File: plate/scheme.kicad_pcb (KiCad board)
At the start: 2 copper layers, 50 x 100 mm, 9 parts

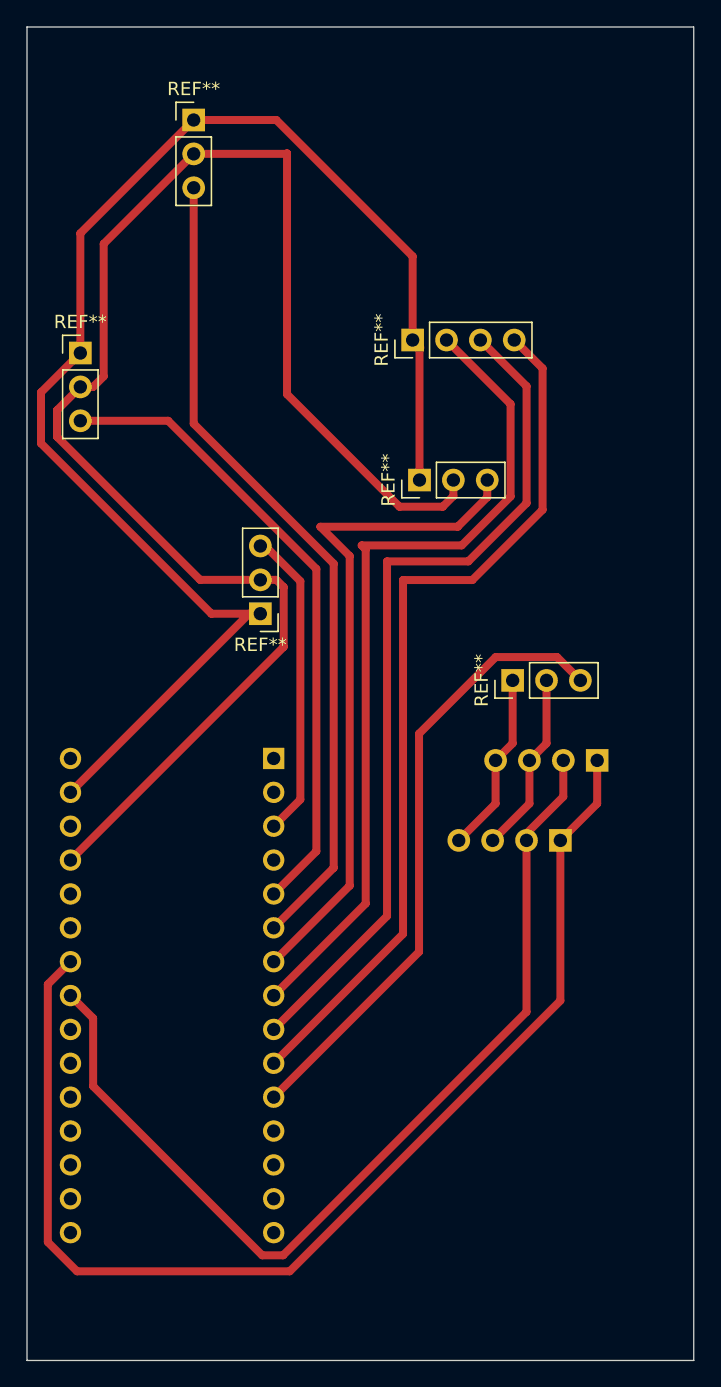
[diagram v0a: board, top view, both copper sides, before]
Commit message: Add new versions of boxes, update readme
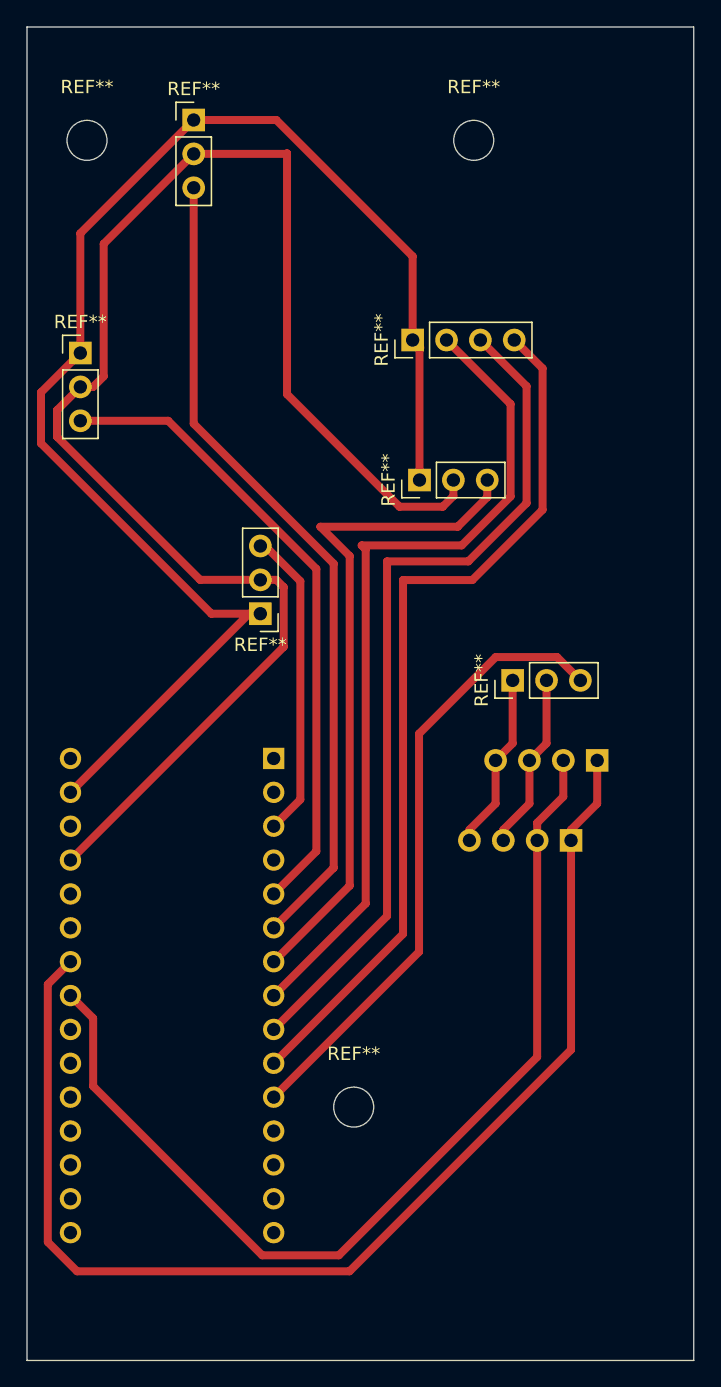
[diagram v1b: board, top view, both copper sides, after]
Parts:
- added REF**: Hole3mm, MountingHole:MountingHole_3mm, F.Cu at (54.5, 28.5)
- added REF**: Hole3mm, MountingHole:MountingHole_3mm, F.Cu at (74.5, 101.0)
- added REF**: Hole3mm, MountingHole:MountingHole_3mm, F.Cu at (83.5, 28.5)
- REF**: value ButtPause -> ButtonPause
- REF**: value Hum -> Humidity
- REF**: value ButtReset -> ButtonReset
- moved REF** 0.80 mm to (90.8, 81.0)
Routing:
- net A5_SCL: track 88.6 -> 91.3 mm
- net A4_SDA: track 72.8 -> 75.3 mm
